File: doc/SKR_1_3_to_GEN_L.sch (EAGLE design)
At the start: 2 parts

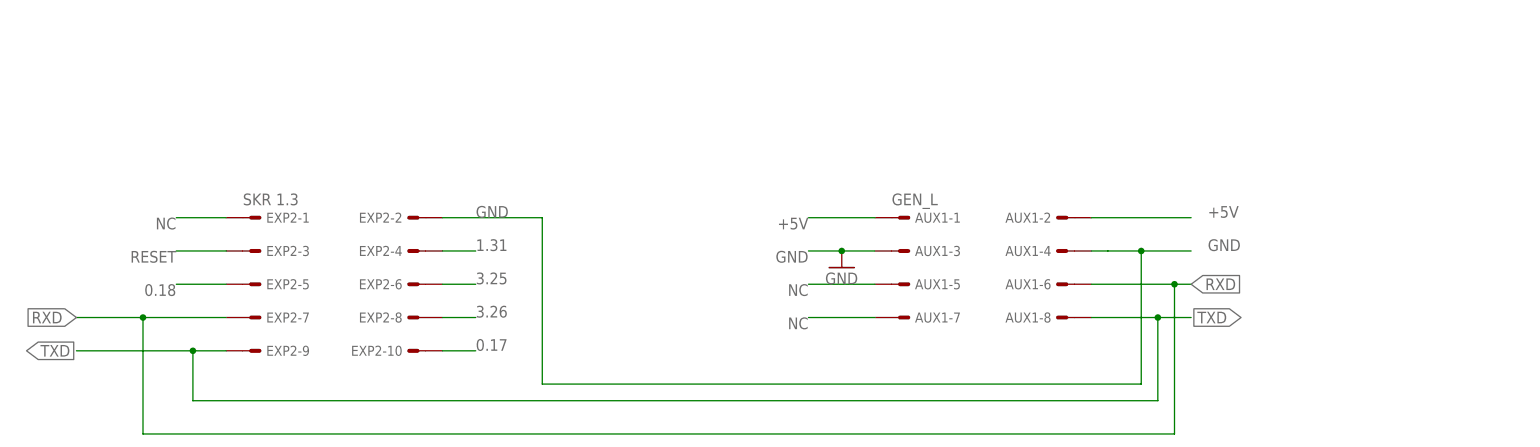
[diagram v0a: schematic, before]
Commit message: updated schematics of connection SKR -> GEN L
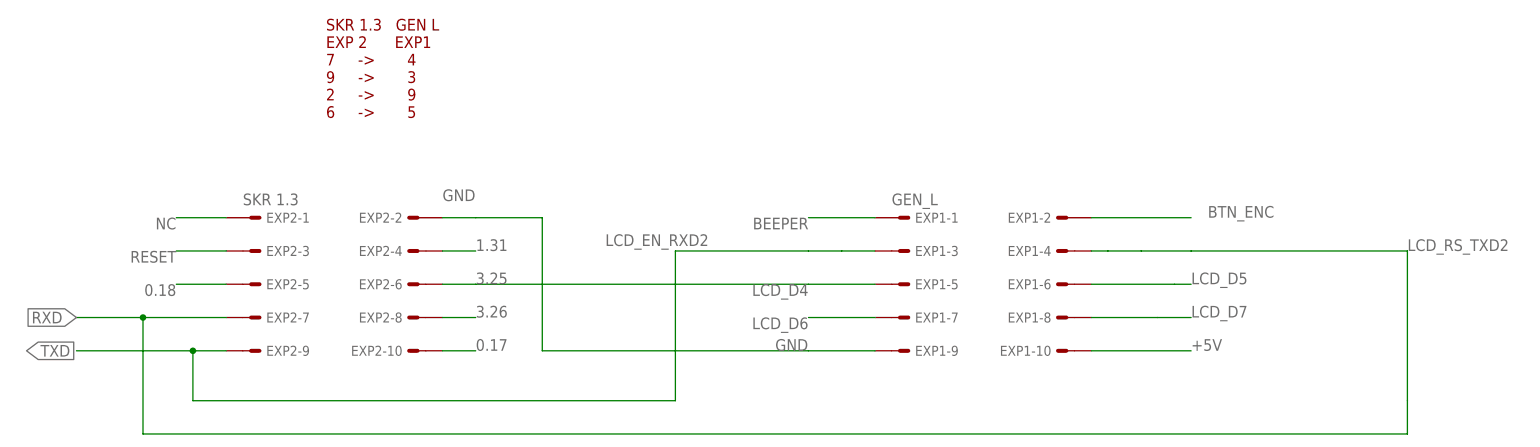
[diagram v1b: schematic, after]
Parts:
- renumbered AUX1 to EXP1
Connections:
- new net BEEPER: EXP1-1.S
- new net BTN_ENC: EXP1-2.S
- new net LCD_D4: EXP1-5.S
- new net LCD_D5: EXP1-6.S
- new net LCD_D6: EXP1-7.S
- new net LCD_D7: EXP1-8.S
- new net LCD_EN_RXD2: EXP1-3.S
- new net LCD_RS_TXD2: EXP1-4.S
- net +5V: now also EXP1-10.S; no longer EXP1-1.S, EXP1-2.S
- net GND: now also EXP1-9.S; no longer EXP1-3.S, EXP1-4.S
- net NC: no longer EXP1-5.S, EXP1-7.S
- net RXD: no longer EXP1-6.S
- net TXD: no longer EXP1-8.S
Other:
- note added: "SKR 1.3 GEN L EXP 2 EXP1 7 -> 4 9 -> 3 2 -> 9 6 -> 5"
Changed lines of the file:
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@@
 <parts>
 <part name="EXP2" library="con-panduit" deviceset="057-010-" device="1" value="SKR 1.3"/>
-<part name="AUX1" library="con-panduit" deviceset="057-010-" device="1" value="GEN_L"/>
-<part name="GND1" library="supply1" deviceset="GND" device=""/>
+<part name="EXP1" library="con-panduit" deviceset="057-010-" device="1" value="GEN_L"/>
 </parts>
 <sheets>
 <sheet>
 <plain>
+<text x="17.78" y="71.12" size="1.778" layer="94">SKR 1.3   GEN L
+EXP 2      EXP1
+7     -&gt;       4
+9     -&gt;       3
+2     -&gt;       9
+6     -&gt;       5</text>
 </plain>
 <instances>
@@
 <instance part="EXP2" gate="-9" x="7.62" y="35.56"/>
 <instance part="EXP2" gate="-10" x="30.48" y="35.56" rot="MR0"/>
-<instance part="AUX1" gate="-1" x="106.68" y="55.88"/>
-<instance part="AUX1" gate="-2" x="129.54" y="55.88" rot="MR0"/>
-<instance part="AUX1" gate="-3" x="106.68" y="50.8"/>
-<instance part="AUX1" gate="-4" x="129.54" y="50.8" rot="MR0"/>
-<instance part="AUX1" gate="-5" x="106.68" y="45.72"/>
-<instance part="AUX1" gate="-6" x="129.54" y="45.72" rot="MR0"/>
-<instance part="AUX1" gate="-7" x="106.68" y="40.64"/>
-<instance part="AUX1" gate="-8" x="129.54" y="40.64" rot="MR0"/>
-<instance part="GND1" gate="1" x="96.52" y="48.26"/>
+<instance part="EXP1" gate="-1" x="106.68" y="55.88"/>
+<instance part="EXP1" gate="-2" x="129.54" y="55.88" rot="MR0"/>
+<instance part="EXP1" gate="-3" x="106.68" y="50.8"/>
+<instance part="EXP1" gate="-4" x="129.54" y="50.8" rot="MR0"/>
+<instance part="EXP1" gate="-5" x="106.68" y="45.72"/>
+<instance part="EXP1" gate="-6" x="129.54" y="45.72" rot="MR0"/>
+<instance part="EXP1" gate="-7" x="106.68" y="40.64"/>
+<instance part="EXP1" gate="-8" x="129.54" y="40.64" rot="MR0"/>
+<instance part="EXP1" gate="-9" x="106.68" y="35.56"/>
+<instance part="EXP1" gate="-10" x="129.54" y="35.56" rot="R180"/>
 </instances>
 <busses>
 </busses>
 <nets>
-<net name="GND" class="0">
-<segment>
-<pinref part="AUX1" gate="-3" pin="S"/>
-<wire x1="101.6" y1="50.8" x2="96.52" y2="50.8" width="0.1524" layer="91"/>
-<label x="91.44" y="50.8" size="1.778" layer="95" rot="R180"/>
-<pinref part="GND1" gate="1" pin="GND"/>
-<wire x1="96.52" y1="50.8" x2="91.44" y2="50.8" width="0.1524" layer="91"/>
-<junction x="96.52" y="50.8"/>
-</segment>
-<segment>
-<pinref part="AUX1" gate="-4" pin="S"/>
-<wire x1="134.62" y1="50.8" x2="137.16" y2="50.8" width="0.1524" layer="91"/>
-<label x="152.4" y="50.8" size="1.778" layer="95"/>
-<wire x1="137.16" y1="50.8" x2="142.24" y2="50.8" width="0.1524" layer="91"/>
-<wire x1="142.24" y1="50.8" x2="149.86" y2="50.8" width="0.1524" layer="91"/>
-<wire x1="142.24" y1="50.8" x2="142.24" y2="30.48" width="0.1524" layer="91"/>
-<pinref part="EXP2" gate="-2" pin="S"/>
-<wire x1="50.8" y1="55.88" x2="35.56" y2="55.88" width="0.1524" layer="91"/>
-<wire x1="142.24" y1="30.48" x2="50.8" y2="30.48" width="0.1524" layer="91"/>
-<wire x1="50.8" y1="30.48" x2="50.8" y2="55.88" width="0.1524" layer="91"/>
-<junction x="142.24" y="50.8"/>
-<label x="40.64" y="55.88" size="1.778" layer="95"/>
-</segment>
-</net>
 <net name="TXD" class="0">
 <segment>
@@
 <wire x1="-2.54" y1="35.56" x2="-20.32" y2="35.56" width="0.1524" layer="91"/>
 <wire x1="-2.54" y1="35.56" x2="-2.54" y2="27.94" width="0.1524" layer="91"/>
-<pinref part="AUX1" gate="-8" pin="S"/>
-<wire x1="134.62" y1="40.64" x2="144.78" y2="40.64" width="0.1524" layer="91"/>
-<wire x1="144.78" y1="40.64" x2="149.86" y2="40.64" width="0.1524" layer="91"/>
-<wire x1="-2.54" y1="27.94" x2="144.78" y2="27.94" width="0.1524" layer="91"/>
-<wire x1="144.78" y1="27.94" x2="144.78" y2="40.64" width="0.1524" layer="91"/>
 <junction x="-2.54" y="35.56"/>
-<junction x="144.78" y="40.64"/>
-<label x="157.48" y="40.64" size="1.778" layer="95" rot="R180" xref="yes"/>
+<wire x1="-2.54" y1="27.94" x2="71.12" y2="27.94" width="0.1524" layer="91"/>
+<wire x1="71.12" y1="27.94" x2="71.12" y2="50.8" width="0.1524" layer="91"/>
+<wire x1="71.12" y1="50.8" x2="91.44" y2="50.8" width="0.1524" layer="91"/>
 </segment>
 </net>
@@
 <wire x1="-10.16" y1="40.64" x2="-20.32" y2="40.64" width="0.1524" layer="91"/>
 <wire x1="-10.16" y1="40.64" x2="-10.16" y2="22.86" width="0.1524" layer="91"/>
-<pinref part="AUX1" gate="-6" pin="S"/>
-<wire x1="134.62" y1="45.72" x2="147.32" y2="45.72" width="0.1524" layer="91"/>
-<wire x1="147.32" y1="45.72" x2="149.86" y2="45.72" width="0.1524" layer="91"/>
-<wire x1="-10.16" y1="22.86" x2="147.32" y2="22.86" width="0.1524" layer="91"/>
-<wire x1="147.32" y1="22.86" x2="147.32" y2="45.72" width="0.1524" layer="91"/>
 <junction x="-10.16" y="40.64"/>
-<junction x="147.32" y="45.72"/>
-<label x="149.86" y="45.72" size="1.778" layer="95" xref="yes"/>
+<wire x1="-10.16" y1="22.86" x2="182.88" y2="22.86" width="0.1524" layer="91"/>
+<wire x1="182.88" y1="22.86" x2="182.88" y2="27.94" width="0.1524" layer="91"/>
+<wire x1="182.88" y1="27.94" x2="182.88" y2="50.8" width="0.1524" layer="91"/>
+<wire x1="182.88" y1="50.8" x2="149.86" y2="50.8" width="0.1524" layer="91"/>
 </segment>
 </net>
@@
 <label x="-5.08" y="55.88" size="1.778" layer="95" rot="R180"/>
 </segment>
-<segment>
-<pinref part="AUX1" gate="-5" pin="S"/>
-<wire x1="101.6" y1="45.72" x2="91.44" y2="45.72" width="0.1524" layer="91"/>
-<label x="91.44" y="45.72" size="1.778" layer="95" rot="R180"/>
-</segment>
-<segment>
-<pinref part="AUX1" gate="-7" pin="S"/>
-<wire x1="101.6" y1="40.64" x2="91.44" y2="40.64" width="0.1524" layer="91"/>
-<label x="91.44" y="40.64" size="1.778" layer="95" rot="R180"/>
-</segment>
 </net>
 <net name="RESET" class="0">
@@
 </segment>
 </net>
-<net name="+5V" class="0">
-<segment>
-<pinref part="AUX1" gate="-1" pin="S"/>
+<net name="BTN_ENC" class="0">
+<segment>
+<pinref part="EXP1" gate="-2" pin="S"/>
+<wire x1="134.62" y1="55.88" x2="149.86" y2="55.88" width="0.1524" layer="91"/>
+<label x="152.4" y="55.88" size="1.778" layer="95"/>
+</segment>
+</net>
+<net name="LCD_RS_TXD2" class="0">
+<segment>
+<wire x1="142.24" y1="50.8" x2="149.86" y2="50.8" width="0.1524" layer="91"/>
+<wire x1="137.16" y1="50.8" x2="142.24" y2="50.8" width="0.1524" layer="91"/>
+<pinref part="EXP1" gate="-4" pin="S"/>
+<wire x1="134.62" y1="50.8" x2="137.16" y2="50.8" width="0.1524" layer="91"/>
+<label x="182.88" y="50.8" size="1.778" layer="95"/>
+</segment>
+</net>
+<net name="LCD_D5" class="0">
+<segment>
+<pinref part="EXP1" gate="-6" pin="S"/>
+<wire x1="134.62" y1="45.72" x2="147.32" y2="45.72" width="0.1524" layer="91"/>
+<wire x1="147.32" y1="45.72" x2="149.86" y2="45.72" width="0.1524" layer="91"/>
+<label x="149.86" y="45.72" size="1.778" layer="95"/>
+</segment>
+</net>
+<net name="LCD_D7" class="0">
+<segment>
+<wire x1="144.78" y1="40.64" x2="149.86" y2="40.64" width="0.1524" layer="91"/>
+<pinref part="EXP1" gate="-8" pin="S"/>
+<wire x1="134.62" y1="40.64" x2="144.78" y2="40.64" width="0.1524" layer="91"/>
+<label x="149.86" y="40.64" size="1.778" layer="95"/>
+</segment>
+</net>
+<net name="BEEPER" class="0">
+<segment>
+<pinref part="EXP1" gate="-1" pin="S"/>
 <wire x1="101.6" y1="55.88" x2="91.44" y2="55.88" width="0.1524" layer="91"/>
 <label x="91.44" y="55.88" size="1.778" layer="95" rot="R180"/>
 </segment>
-<segment>
-<pinref part="AUX1" gate="-2" pin="S"/>
-<wire x1="134.62" y1="55.88" x2="149.86" y2="55.88" width="0.1524" layer="91"/>
-<label x="152.4" y="55.88" size="1.778" layer="95"/>
+</net>
+<net name="LCD_EN_RXD2" class="0">
+<segment>
+<pinref part="EXP1" gate="-3" pin="S"/>
+<wire x1="101.6" y1="50.8" x2="96.52" y2="50.8" width="0.1524" layer="91"/>
+<label x="76.2" y="53.34" size="1.778" layer="95" rot="R180"/>
+<wire x1="96.52" y1="50.8" x2="91.44" y2="50.8" width="0.1524" layer="91"/>
+</segment>
+</net>
+<net name="LCD_D4" class="0">
+<segment>
+<pinref part="EXP1" gate="-5" pin="S"/>
+<wire x1="101.6" y1="45.72" x2="91.44" y2="45.72" width="0.1524" layer="91"/>
+<label x="91.44" y="45.72" size="1.778" layer="95" rot="R180"/>
+<wire x1="91.44" y1="45.72" x2="40.64" y2="45.72" width="0.1524" layer="91"/>
+</segment>
+</net>
+<net name="LCD_D6" class="0">
+<segment>
+<pinref part="EXP1" gate="-7" pin="S"/>
+<wire x1="101.6" y1="40.64" x2="91.44" y2="40.64" width="0.1524" layer="91"/>
+<label x="91.44" y="40.64" size="1.778" layer="95" rot="R180"/>
+</segment>
+</net>
+<net name="GND" class="0">
+<segment>
+<pinref part="EXP2" gate="-2" pin="S"/>
+<wire x1="35.56" y1="55.88" x2="40.64" y2="55.88" width="0.1524" layer="91"/>
+<label x="35.56" y="58.42" size="1.778" layer="95"/>
+<wire x1="40.64" y1="55.88" x2="50.8" y2="55.88" width="0.1524" layer="91"/>
+<wire x1="50.8" y1="55.88" x2="50.8" y2="35.56" width="0.1524" layer="91"/>
+<pinref part="EXP1" gate="-9" pin="S"/>
+<wire x1="101.6" y1="35.56" x2="91.44" y2="35.56" width="0.1524" layer="91"/>
+<label x="86.36" y="35.56" size="1.778" layer="95"/>
+<wire x1="50.8" y1="35.56" x2="91.44" y2="35.56" width="0.1524" layer="91"/>
+</segment>
+</net>
+<net name="+5V" class="0">
+<segment>
+<pinref part="EXP1" gate="-10" pin="S"/>
+<wire x1="134.62" y1="35.56" x2="149.86" y2="35.56" width="0.1524" layer="91"/>
+<label x="149.86" y="35.56" size="1.778" layer="95"/>
 </segment>
 </net>
@@
 </schematic>
 </drawing>
+<compatibility>
+<note version="6.3" minversion="6.2.2" severity="warning">
+Since Version 6.2.2 text objects can contain more than one line,
+which will not be processed correctly with this version.
+</note>
+</compatibility>
 </eagle>
